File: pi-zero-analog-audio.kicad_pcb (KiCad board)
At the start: 2 copper layers, 65 x 30 mm, 33 parts, among them J1 GPIO, J2 SJ1-3555NG-BE, J3 Screw_Terminal_01x04, U1 LP5907MFX-3.3, U2 74LVC2G34, U3 PAM8403D

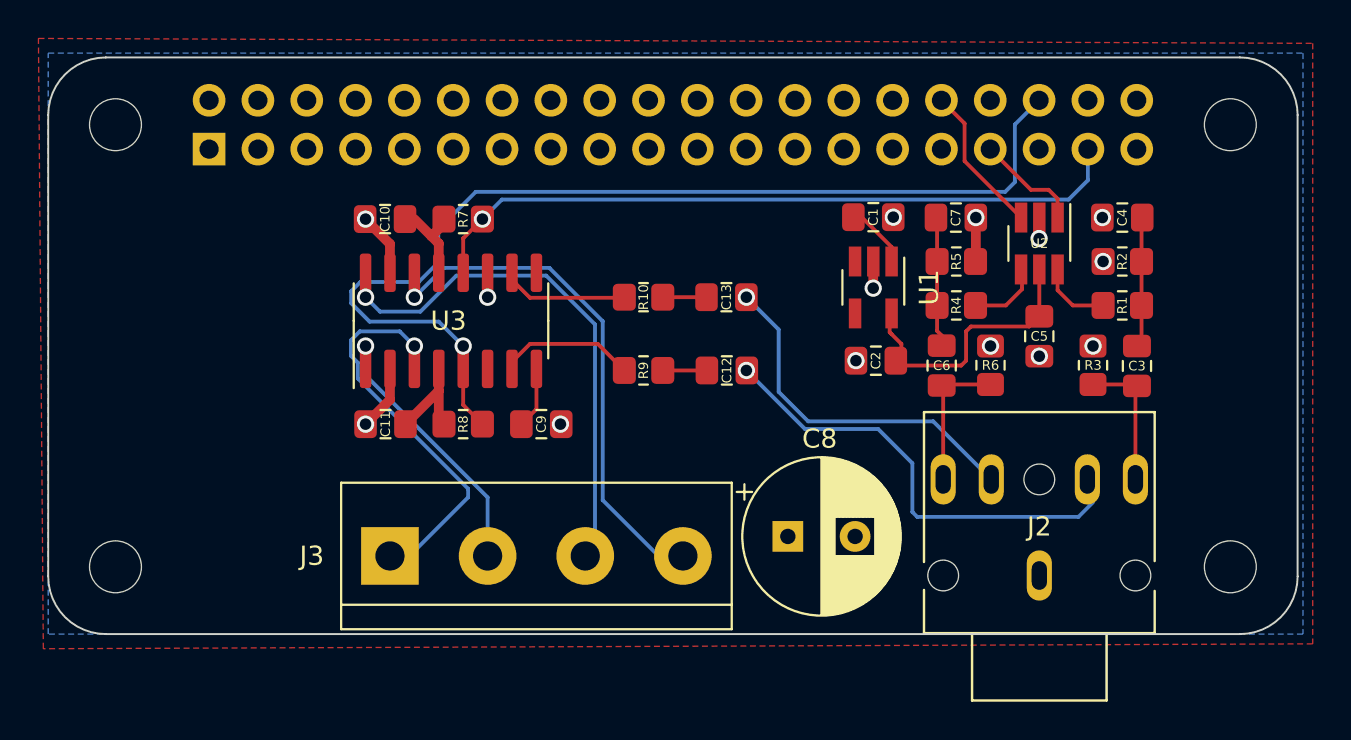
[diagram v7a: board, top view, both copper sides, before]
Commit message: rewrite to components that I actually can have
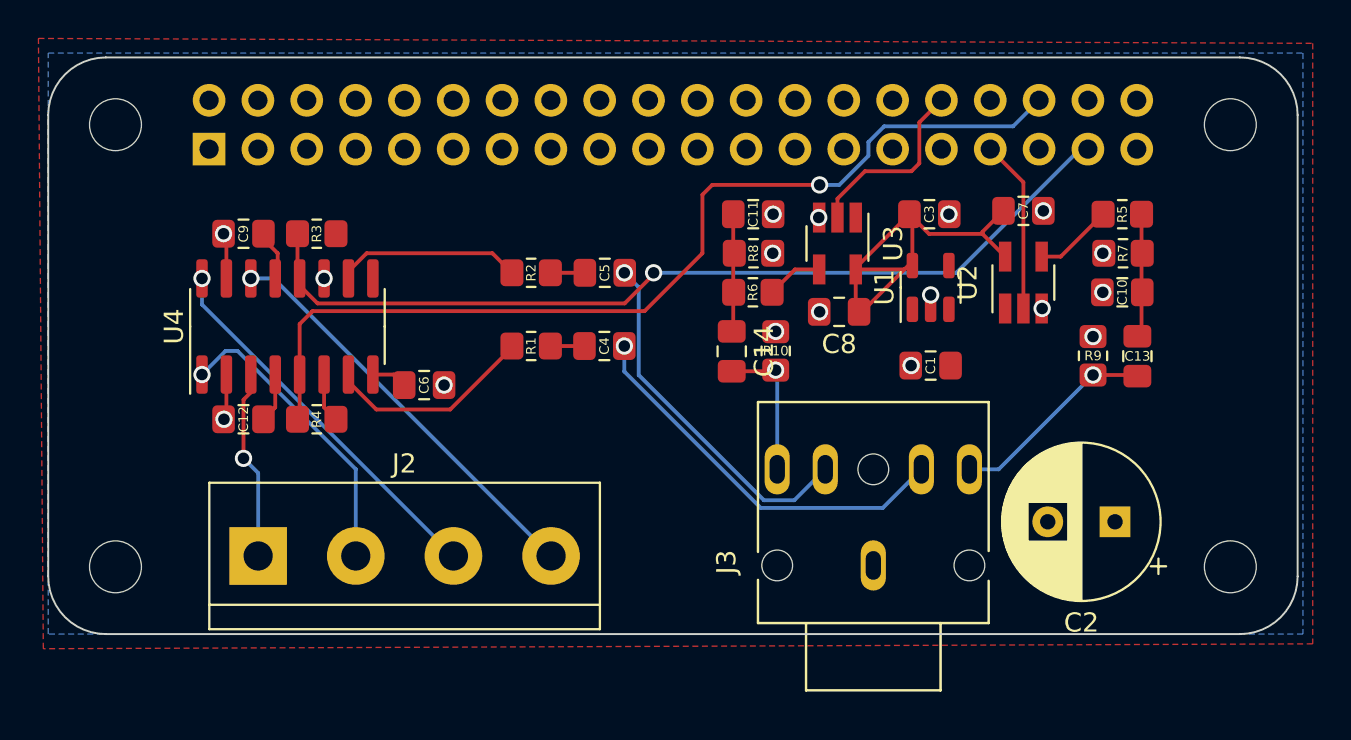
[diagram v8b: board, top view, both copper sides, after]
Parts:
- added C14: 47u, Capacitor_SMD:C_0805_2012Metric_Pad1.18x1.45mm_HandSolder, F.Cu at (135.6, 85.3)
- added U4: PAM8403D, Package_SO:SOP-16_3.9x9.9mm_P1.27mm, F.Cu at (112.4, 84.0)
- C10, C11: value 1u -> 100n
- C12: value 470n -> 1u
- C13: value 470n -> 47u
- C2: value 4.7u -> 470u; footprint Capacitor_SMD:C_0805_2012Metric_Pad1.18x1.45mm_HandSolder -> Capacitor_THT:CP_Radial_D8.0mm_P3.50mm
- C3: value 47u -> 4.7u
- C4, C5: value 100n -> 470n
- C6: value 47u -> 100n
- C8: value 470u -> 100n; footprint Capacitor_THT:CP_Radial_D8.0mm_P3.50mm -> Capacitor_SMD:C_0805_2012Metric_Pad1.18x1.45mm_HandSolder
- C9: value 100n -> 1u
- J2: value SJ1-3555NG-BE -> Screw_Terminal_01x04; footprint library:CUI_SJ1-3555NG-BE -> TerminalBlock:TerminalBlock_bornier-4_P5.08mm
- J3: value Screw_Terminal_01x04 -> SJ1-3555NG-BE; footprint TerminalBlock:TerminalBlock_bornier-4_P5.08mm -> library:CUI_SJ1-3555NG-BE
- R1: value 220R -> 140k
- R10, R9: value 140k -> 1.8k
- R2: value 100R -> 140k
- R3: value 1.8k -> 10k
- R4: value 220R -> 10K
- R5: value 100R -> 220R
- R6: value 1.8k -> 220R
- R7: value 10k -> 100R
- R8: value 10K -> 100R
- U1: value LP5907MFX-3.3 -> MIC5365-3.3YD5; footprint Package_TO_SOT_SMD:SOT-23-5_HandSoldering -> Package_TO_SOT_SMD:SOT-23-5
- U2: value 74LVC2G34 -> MC74VHC1GT50; footprint Package_TO_SOT_SMD:SOT-23-6_Handsoldering -> Package_TO_SOT_SMD:SOT-23-5_HandSoldering
- U3: value PAM8403D -> MC74VHC1GT50; footprint Package_SO:SOP-16_3.9x9.9mm_P1.27mm -> Package_TO_SOT_SMD:SOT-23-5_HandSoldering
- moved R3 41.0 mm to (114.0, 79.2), turned to 0 degrees
- moved J2 40.7 mm to (110.9, 95.9), turned to 0 degrees
- moved C10 38.5 mm to (155.9, 82.2), turned to 180 degrees
- moved R7 34.4 mm to (155.9, 80.2)
- moved R4 33.8 mm to (114.0, 88.8)
- moved R1 30.8 mm to (125.1, 85.0), turned to 0 degrees
- moved R2 30.8 mm to (125.1, 81.2), turned to 0 degrees
- moved C4 27.8 mm to (128.9, 85.0), turned to 0 degrees
- moved C6 26.9 mm to (119.6, 87.0), turned to 0 degrees
- moved C12 25.3 mm to (110.2, 88.8)
- moved J3 25.2 mm to (142.9, 96.4), turned to 90 degrees
- moved R9 23.4 mm to (154.4, 85.5), turned to 90 degrees
- moved C5 22.8 mm to (129.0, 81.2), turned to 0 degrees
- moved C11 22.0 mm to (136.7, 78.2)
- moved C13 21.6 mm to (156.7, 85.5), turned to -90 degrees
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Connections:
- C10 pad 1: GND -> Net-(C10-Pad1)
- C10 pad 2: +5V -> GND
- C11 pad 1: GND -> Net-(C11-Pad1)
- C11 pad 2: +5V -> GND
- C12 pad 1: Net-(C12-Pad1) -> GND
- C12 pad 2: /AMP_L -> +5V
- C13 pad 1: Net-(C13-Pad1) -> Net-(C10-Pad1)
- C13 pad 2: /AMP_R -> /AUDIO_L
- C2 pad 1: VCC -> +5V
- C3 pad 1: Net-(C3-Pad1) -> /AUD_3V3
- C3 pad 2: /AUDIO_L -> GND
- C4 pad 1: Net-(C3-Pad1) -> Net-(C4-Pad1)
- C4 pad 2: GND -> /AMP_L
- C5 pad 1: VCC -> Net-(C5-Pad1)
- C5 pad 2: GND -> /AMP_R
- C6 pad 2: /AUDIO_R -> GND
- C7 pad 1: Net-(C6-Pad1) -> /AUD_3V3
- C8 pad 1: +5V -> /AUD_3V3
- C9 pad 1: Net-(C9-Pad1) -> GND
- C9 pad 2: GND -> +5V
- J2 pad 1: GND -> /L-
- J2 pad 2: /AUDIO_L -> /L+
- J2 pad 3: /AUDIO_R -> /R+
- J2 pad 4: /AMP_L -> /R-
- J3 pad 1: /L- -> GND
- J3 pad 2: /L+ -> /AUDIO_L
- J3 pad 3: /R+ -> /AUDIO_R
- J3 pad 4: /R- -> /AMP_L
- R1 pad 1: Net-(C3-Pad1) -> Net-(R1-Pad1)
- R1 pad 2: Net-(R1-Pad2) -> Net-(C4-Pad1)
- R10 pad 1: Net-(R10-Pad1) -> /AUDIO_R
- R10 pad 2: Net-(C13-Pad1) -> GND
- R2 pad 1: Net-(C3-Pad1) -> Net-(R2-Pad1)
- R2 pad 2: GND -> Net-(C5-Pad1)
- R3 pad 1: /AUDIO_L -> /SHDN
- R3 pad 2: GND -> +5V
- R4 pad 1: Net-(C6-Pad1) -> /MUTE
- R4 pad 2: Net-(R4-Pad2) -> +5V
- R5 pad 1: Net-(C6-Pad1) -> Net-(C10-Pad1)
- R5 pad 2: GND -> Net-(R5-Pad2)
- R6 pad 1: /AUDIO_R -> Net-(C11-Pad1)
- R6 pad 2: GND -> Net-(R6-Pad2)
- R7 pad 1: /SHDN -> Net-(C10-Pad1)
- R7 pad 2: +5V -> GND
- R8 pad 1: /MUTE -> Net-(C11-Pad1)
- R8 pad 2: +5V -> GND
- R9 pad 1: Net-(R9-Pad1) -> /AUDIO_L
- R9 pad 2: Net-(C12-Pad1) -> GND
- U1 pad 5: VCC -> /AUD_3V3
- U2 pad 1: /PWM1 -> unconnected-(U2-Pad1)
- U2 pad 2: GND -> /PWM1
- U2 pad 3: /PWM0 -> GND
- U2 pad 4: Net-(R4-Pad2) -> Net-(R5-Pad2)
- U2 pad 5: VCC -> /AUD_3V3
- U3 pad 1: /L+ -> unconnected-(U3-Pad1)
- U3 pad 2: GND -> /PWM0
- U3 pad 3: /L- -> GND
- U3 pad 4: +5V -> Net-(R6-Pad2)
- U3 pad 5: /MUTE -> /AUD_3V3
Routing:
- net /AUD_3V3: track 0.00 -> 22.1 mm
- net VCC: track 13.6 -> 0.00 mm
- net Net-(R1-Pad1): track 0.00 -> 10.4 mm
- net /SHDN: track 37.2 -> 46.6 mm
- net Net-(R2-Pad1): track 0.00 -> 9.32 mm
- net /L-: track 18.8 -> 9.91 mm
- net Net-(R9-Pad1): track 6.80 -> 0.00 mm
- net Net-(R10-Pad1): track 6.20 -> 0.00 mm
- net Net-(C10-Pad1): track 0.00 -> 6.13 mm
- net Net-(C11-Pad1): track 0.00 -> 6.02 mm
- net +5V: track 13.4 -> 7.39 mm
- net GND: track 10.4 -> 4.38 mm, vias 14 -> 17
- net Net-(C3-Pad1): track 5.85 -> 0.00 mm
- net /R+: track 25.6 -> 19.9 mm
- net Net-(C6-Pad1): track 6.70 -> 1.86 mm
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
